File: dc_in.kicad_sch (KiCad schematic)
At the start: 4 parts

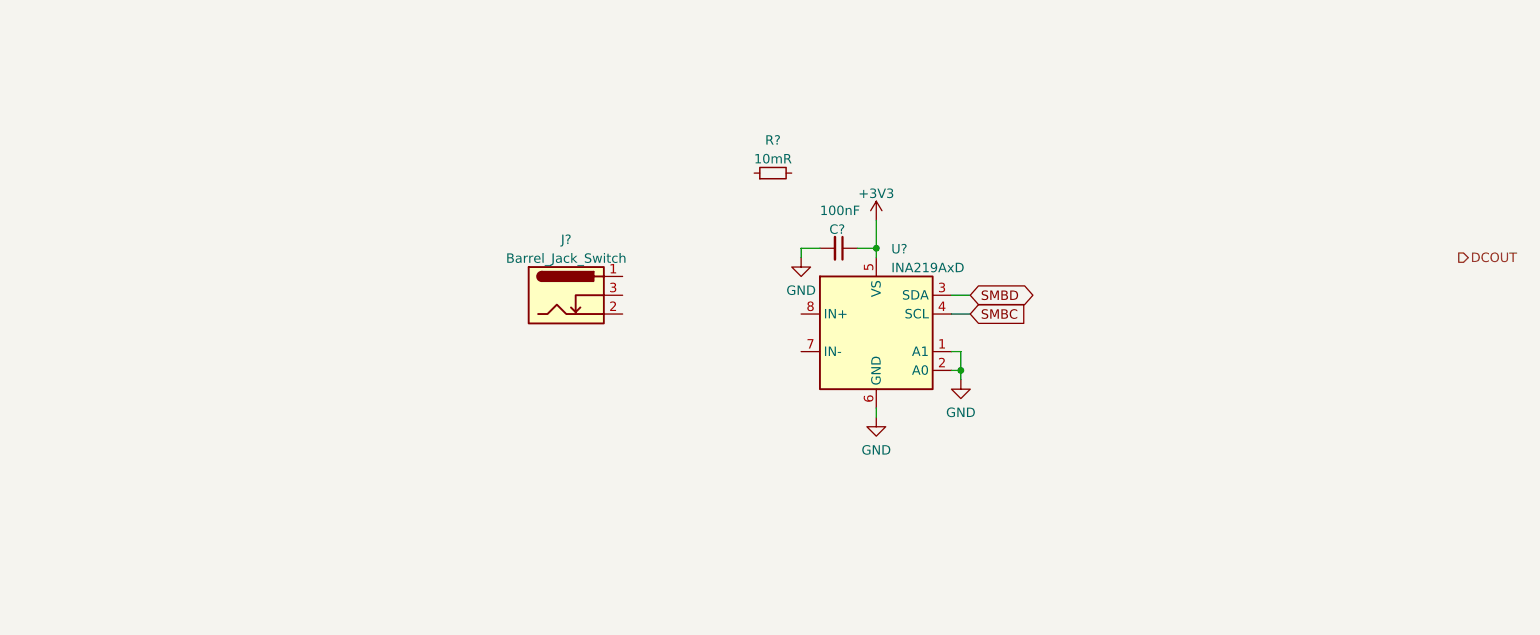
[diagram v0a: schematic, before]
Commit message: Add partial DC output circuitry
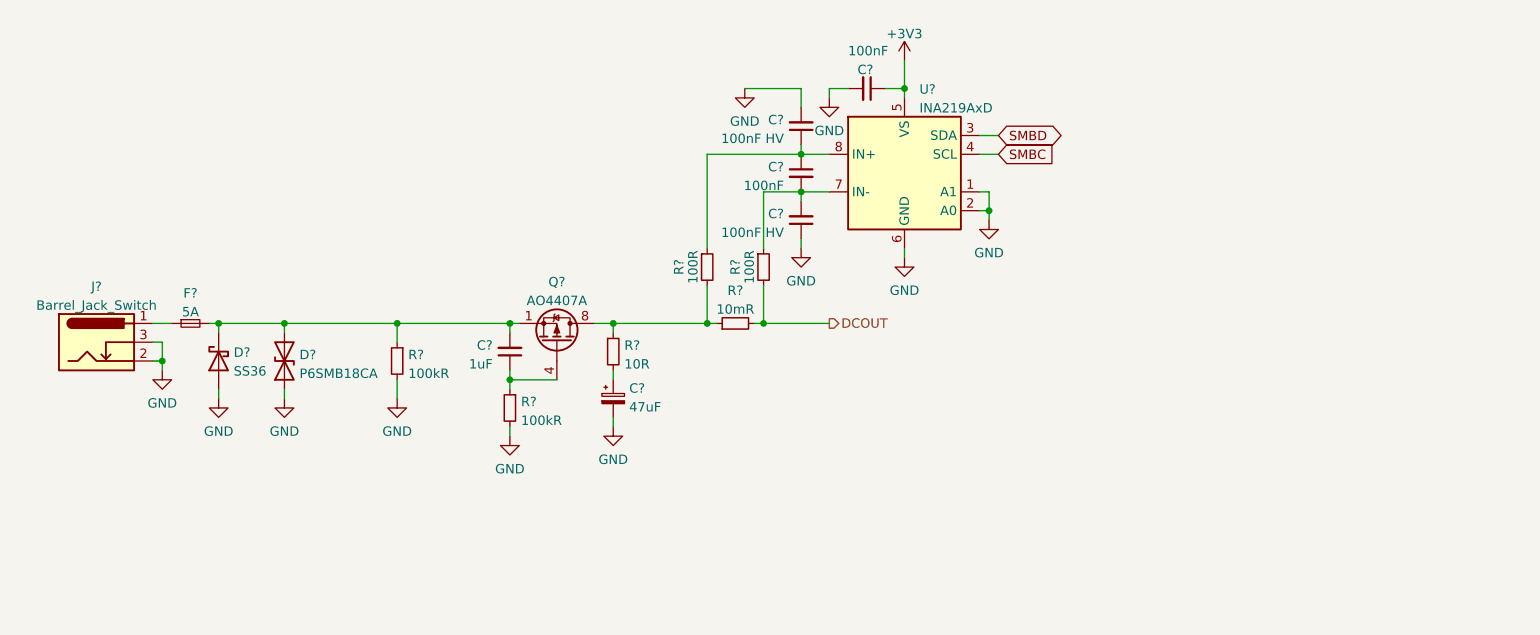
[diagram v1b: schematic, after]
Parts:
- added C? (x2): 100nF HV, Capacitor_SMD:C_0603_1608Metric, symbol Device:C_Small
- added C?: 100nF, Capacitor_SMD:C_0402_1005Metric, symbol Device:C_Small
- added C?: 1uF, Capacitor_SMD:C_0402_1005Metric, symbol Device:C_Small
- added C?: 47uF, Capacitor_SMD:CP_Elec_6.3x5.4, symbol Device:C_Polarized_Small
- added D?: P6SMB18CA, Diode_SMD:D_SMB, symbol Device:D_TVS
- added D?: SS36, Diode_SMD:D_SMC, symbol Device:D_Schottky
- added F?: 5A, Fuse:Fuse_1206_3216Metric, symbol Device:Fuse_Small
- added Q?: AO4407A, Package_SO:SOIC-8_3.9x4.9mm_P1.27mm, symbol Transistor_FET:FDS9435A
- added R? (x2): 100kR, Resistor_SMD:R_0402_1005Metric, symbol Device:R_Small
- added R? (x2): 100R, Resistor_SMD:R_0402_1005Metric, symbol Device:R_Small
- added R?: 10R, Resistor_SMD:R_1206_3216Metric, symbol Device:R_Small
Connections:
- net DCOUT: now also R?.2, R?.2
- net GND: now also J?.2, J?.3, C?.1, C?.2, C?.2, D?.1 (A1), D?.2 (A), R?.2, R?.2
- net at J?.1: now also F?.1
- net at U?.7 (IN-): now also C?.2, C?.2, R?.1
- net at U?.8 (IN+): now also C?.1, C?.1, R?.1
- net at R?.1: now also Q?.5 (D), Q?.6 (D), Q?.7 (D), Q?.8 (D), R?.1, R?.2
- new net: C?.1, Q?.4 (G), R?.1
- new net: C?.2, D?.1 (K), D?.2 (A2), F?.2, Q?.1 (S), Q?.2 (S), Q?.3 (S), R?.1
- new net: C?.1, R?.2
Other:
- moved on the sheet: C?, J?, R?, U?

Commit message: Finish DC output schematic capture
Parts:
- removed C?: 47uF, Capacitor_SMD:CP_Elec_6.3x5.4, symbol Device:C_Polarized_Small
- removed U?: INA219AxD, Package_SO:SOIC-8_3.9x4.9mm_P1.27mm, symbol Analog_ADC:INA219AxD
- added C?: 220uF, Capacitor_SMD:CP_Elec_6.3x7.7, symbol Device:C_Polarized_Small
- added U?: INA219AxD, Package_SO:SOIC-8_3.9x4.9mm_P1.27mm, symbol Analog_ADC:INA219AxD
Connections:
- net +3V3: now also U?.5 (VS)
- net GND: now also C?.2, U?.1 (A1), U?.2 (A0), U?.6 (GND)
- net SMBC: now also U?.4 (SCL)
- net SMBD: now also U?.3 (SDA)
- net at C?.2, C?.2, R?.1: now also U?.7 (IN-)
- net at C?.1, C?.1, R?.1: now also U?.8 (IN+)
- net at R?.2: now also C?.1
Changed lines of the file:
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@@
     (pin "2")
-  )
-  (symbol (lib_id "Connector:Barrel_Jack_Switch") (at 34.29 97.79 0) (unit 1)
-    (in_bom yes) (on_board yes) (fields_autoplaced)
-    (property "Reference" "J?" (id 0) (at 34.29 90.2802 0))
-    (property "Value" "Barrel_Jack_Switch" (id 1) (at 34.29 92.8171 0))
-    (property "Footprint" "" (id 2) (at 35.56 98.806 0)
-      (effects (font (size 1.27 1.27)) hide)
-    )
-    (property "Datasheet" "~" (id 3) (at 35.56 98.806 0)
-      (effects (font (size 1.27 1.27)) hide)
-    )
-    (pin "1")
-    (pin "2")
-    (pin "3")
   )
   (symbol (lib_id "Analog_ADC:INA219AxD") (at 143.51 74.93 0) (unit 1)
@@
     )
     (property "Datasheet" "http://www.ti.com/lit/ds/symlink/ina219.pdf" (id 3) (at 152.4 77.47 0)
+      (effects (font (size 1.27 1.27)) hide)
+    )
+    (property "LCSC" "C138706" (id 4) (at 143.51 74.93 0)
       (effects (font (size 1.27 1.27)) hide)
     )
@@
     (pin "8")
   )
+  (symbol (lib_id "Connector:Barrel_Jack_Switch") (at 34.29 97.79 0) (unit 1)
+    (in_bom yes) (on_board yes) (fields_autoplaced)
+    (property "Reference" "J?" (id 0) (at 34.29 90.2802 0))
+    (property "Value" "Barrel_Jack_Switch" (id 1) (at 34.29 92.8171 0))
+    (property "Footprint" "" (id 2) (at 35.56 98.806 0)
+      (effects (font (size 1.27 1.27)) hide)
+    )
+    (property "Datasheet" "~" (id 3) (at 35.56 98.806 0)
+      (effects (font (size 1.27 1.27)) hide)
+    )
+    (pin "1")
+    (pin "2")
+    (pin "3")
+  )
   (symbol (lib_id "power:GND") (at 104.14 109.22 0) (unit 1)
     (in_bom yes) (on_board yes) (fields_autoplaced)
@@
     (pin "1")
   )
+  (symbol (lib_id "Device:C_Polarized_Small") (at 104.14 105.41 0) (unit 1)
+    (in_bom yes) (on_board yes) (fields_autoplaced)
+    (property "Reference" "C?" (id 0) (at 106.299 104.0292 0)
+      (effects (font (size 1.27 1.27)) (justify left))
+    )
+    (property "Value" "220uF" (id 1) (at 106.299 106.5661 0)
+      (effects (font (size 1.27 1.27)) (justify left))
+    )
+    (property "Footprint" "Capacitor_SMD:CP_Elec_6.3x7.7" (id 2) (at 104.14 105.41 0)
+      (effects (font (size 1.27 1.27)) hide)
+    )
+    (property "Datasheet" "https://datasheet.lcsc.com/lcsc/1912111437_Nichicon-UCM1E221MCL1GS_C340768.pdf" (id 3) (at 104.14 105.41 0)
+      (effects (font (size 1.27 1.27)) hide)
+    )
+    (property "LCSC" "C340768" (id 4) (at 104.14 105.41 0)
+      (effects (font (size 1.27 1.27)) hide)
+    )
+    (pin "1")
+    (pin "2")
+  )
   (symbol (lib_id "power:GND") (at 143.51 86.36 0) (unit 1)
     (in_bom yes) (on_board yes) (fields_autoplaced)
@@
     (pin "1")
   )
-  (symbol (lib_id "Device:C_Polarized_Small") (at 104.14 105.41 0) (unit 1)
-    (in_bom yes) (on_board yes) (fields_autoplaced)
-    (property "Reference" "C?" (id 0) (at 106.299 104.0292 0)
-      (effects (font (size 1.27 1.27)) (justify left))
-    )
-    (property "Value" "47uF" (id 1) (at 106.299 106.5661 0)
-      (effects (font (size 1.27 1.27)) (justify left))
-    )
-    (property "Footprint" "Capacitor_SMD:CP_Elec_6.3x5.4" (id 2) (at 104.14 105.41 0)
-      (effects (font (size 1.27 1.27)) hide)
-    )
-    (property "Datasheet" "https://datasheet.lcsc.com/lcsc/2010160904_ROQANG-RVT1V470M0605_C72522.pdf" (id 3) (at 104.14 105.41 0)
-      (effects (font (size 1.27 1.27)) hide)
-    )
-    (property "LCSC" "C72522" (id 4) (at 104.14 105.41 0)
-      (effects (font (size 1.27 1.27)) hide)
-    )
-    (pin "1")
-    (pin "2")
-  )
   (symbol (lib_id "power:GND") (at 59.69 105.41 0) (unit 1)

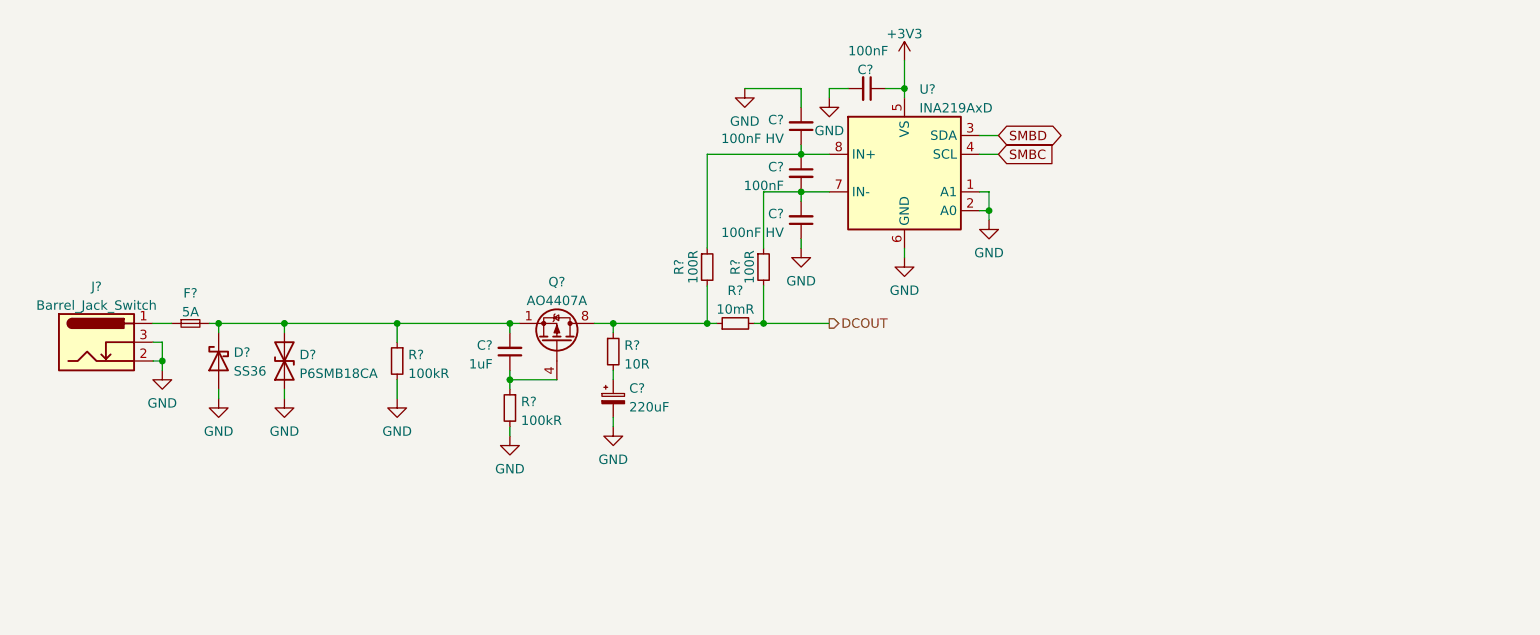
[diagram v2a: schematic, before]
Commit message: Add barrel jack footprints
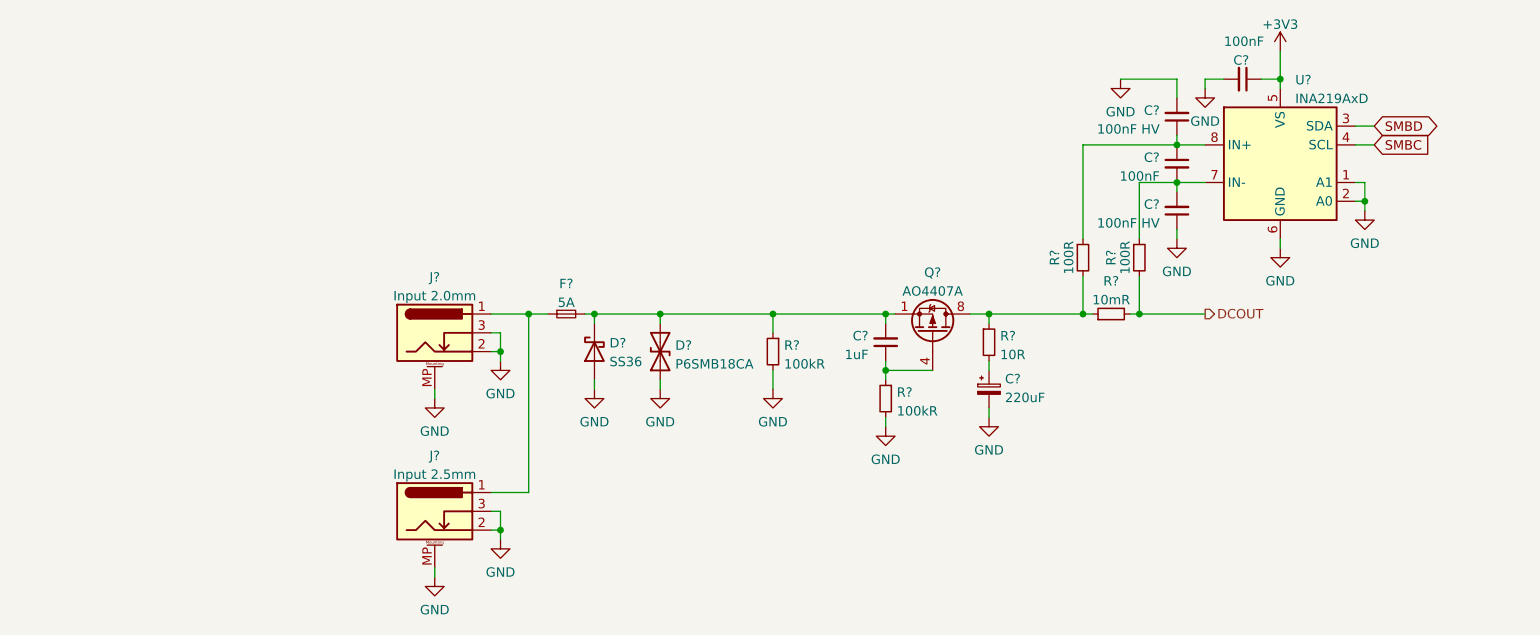
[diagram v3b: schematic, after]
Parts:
- removed J?: Barrel_Jack_Switch, symbol Connector:Barrel_Jack_Switch
- added J?: Input 2.0mm, Connector_BarrelJack_LCSC:BarrelJack_2.0mm_DC-044B, symbol Connector:Barrel_Jack_Switch_MountingPin
- added J?: Input 2.5mm, Connector_BarrelJack_LCSC:BarrelJack_2.0mm_DC-044B, symbol Connector:Barrel_Jack_Switch_MountingPin
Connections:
- net GND: now also J?.2, J?.2, J?.3, J?.3, J?.MP (MountPin), J?.MP (MountPin)
- net at F?.1: now also J?.1, J?.1
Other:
- moved on the sheet: C?, D?, F?, Q?, R?, U?

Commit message: Add individually switchable outputs
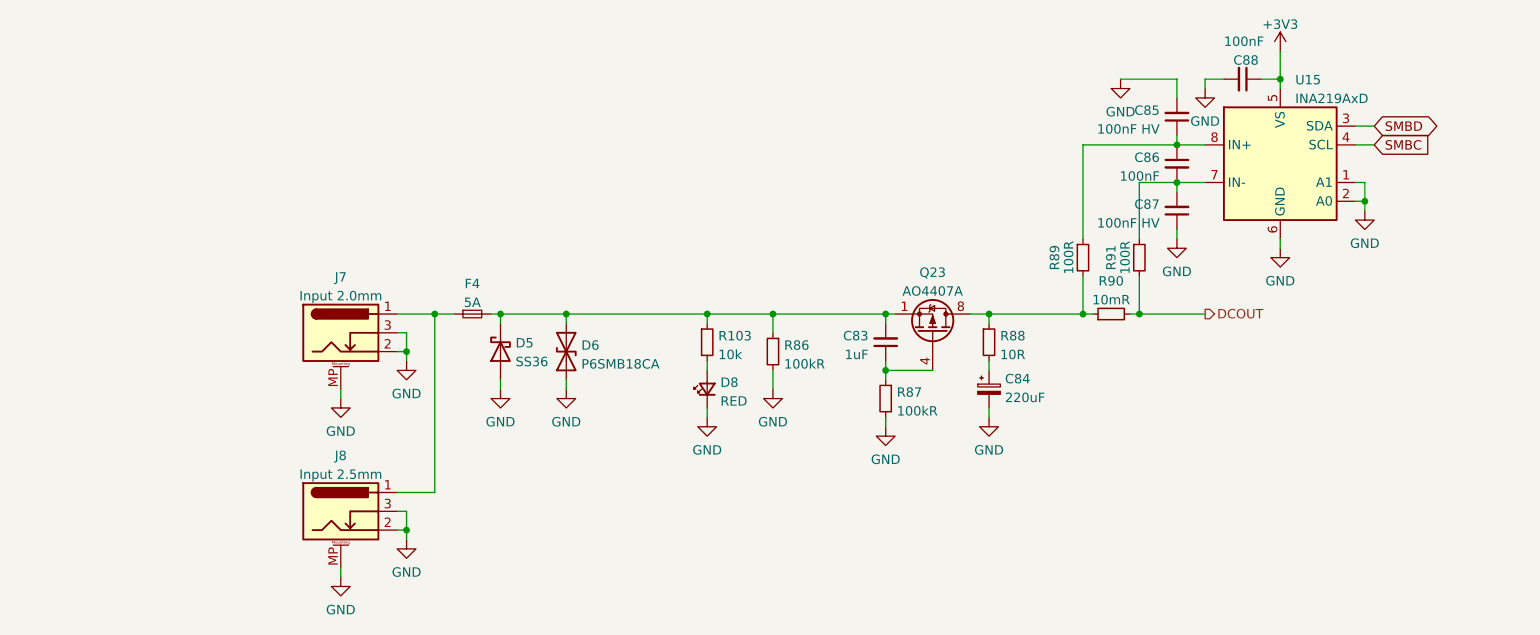
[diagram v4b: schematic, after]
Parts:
- added D8: RED, LED_Indicator:LED_Indicator_RED_MHK1373CRBDT, symbol Device:LED_Small
- added R103: 10k, Resistor_SMD:R_0402_1005Metric, symbol Device:R_Small
- J8: renamed from J?; footprint Connector_BarrelJack_LCSC:BarrelJack_2.0mm_DC-044B -> Connector_BarrelJack_LCSC:BarrelJack_2.5mm_DC-044K-D025
- gave numbers to parts that had none: 18
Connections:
- net GND: now also D8.1 (K)
- net at C83.2, D5.1 (K), D6.2 (A2)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: now also R103.1
- new net: D8.2 (A), R103.2
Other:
- moved on the sheet: D5, D6, F4, J7, J8

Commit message: Partial layout
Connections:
- net DCSMOOTH: now reaches Q23.5 (D), Q23.6 (D), Q23.7 (D), Q23.8 (D), R88.1, R89.2, R90.1
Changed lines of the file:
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@@
     (stroke (width 0) (type default) (color 0 0 0 0))
+  )
+  (label "DCSMOOTH" (at 154.94 93.98 0)
+    (effects (font (size 1.27 1.27)) (justify left bottom))
   )
   (global_label "SMBD" (shape bidirectional) (at 207.01 68.58 0) (fields_autoplaced)

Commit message: Fix footprint origins for JLC assembly
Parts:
- Q23: LCSC C16072 -> C35349
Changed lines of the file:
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@@
       (effects (font (size 1.27 1.27) italic) (justify left) hide)
     )
-    (property "Datasheet" "https://datasheet.lcsc.com/szlcsc/Alpha-Omega-Semicon-AOS-AO4407A_C16072.pdf" (id 3) (at 147.32 96.52 90)
+    (property "Datasheet" "https://datasheet.lcsc.com/szlcsc/Alpha-Omega-Semicon-AOS-AO4407A_C35349.pdf" (id 3) (at 147.32 96.52 90)
       (effects (font (size 1.27 1.27)) (justify left) hide)
     )
-    (property "LCSC" "C16072" (id 4) (at 147.32 96.52 0)
+    (property "LCSC" "C35349" (id 4) (at 147.32 96.52 0)
       (effects (font (size 1.27 1.27)) hide)
     )

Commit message: Fix incorrect AO447A partnumber
The previous partnumber was pointing to a N-Channel MOSFET.
Use a P-Channel one.
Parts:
- Q23: LCSC C35349 -> C167517
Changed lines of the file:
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@@
       (effects (font (size 1.27 1.27)) (justify left) hide)
     )
-    (property "LCSC" "C35349" (id 4) (at 147.32 96.52 0)
+    (property "LCSC" "C167517" (id 4) (at 147.32 96.52 0)
       (effects (font (size 1.27 1.27)) hide)
     )

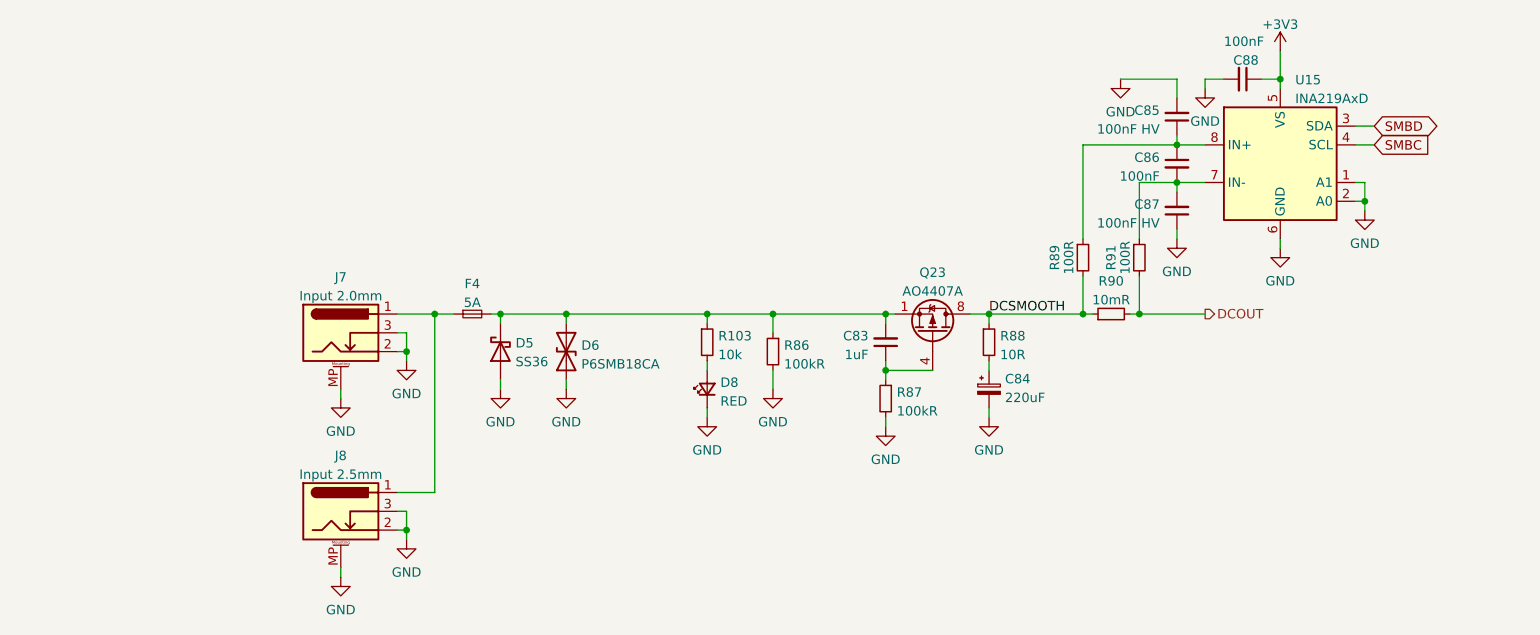
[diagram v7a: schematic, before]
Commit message: Rev 1.0 bugfixes
Changes:
 - Replace DCOK-driven DC passthrough switch with ideal diode
 - Reduce INA219 series filter resistance to 1 ohm
 - Simplify debug USB power gating
 - Fix incorrect USB CC pullups
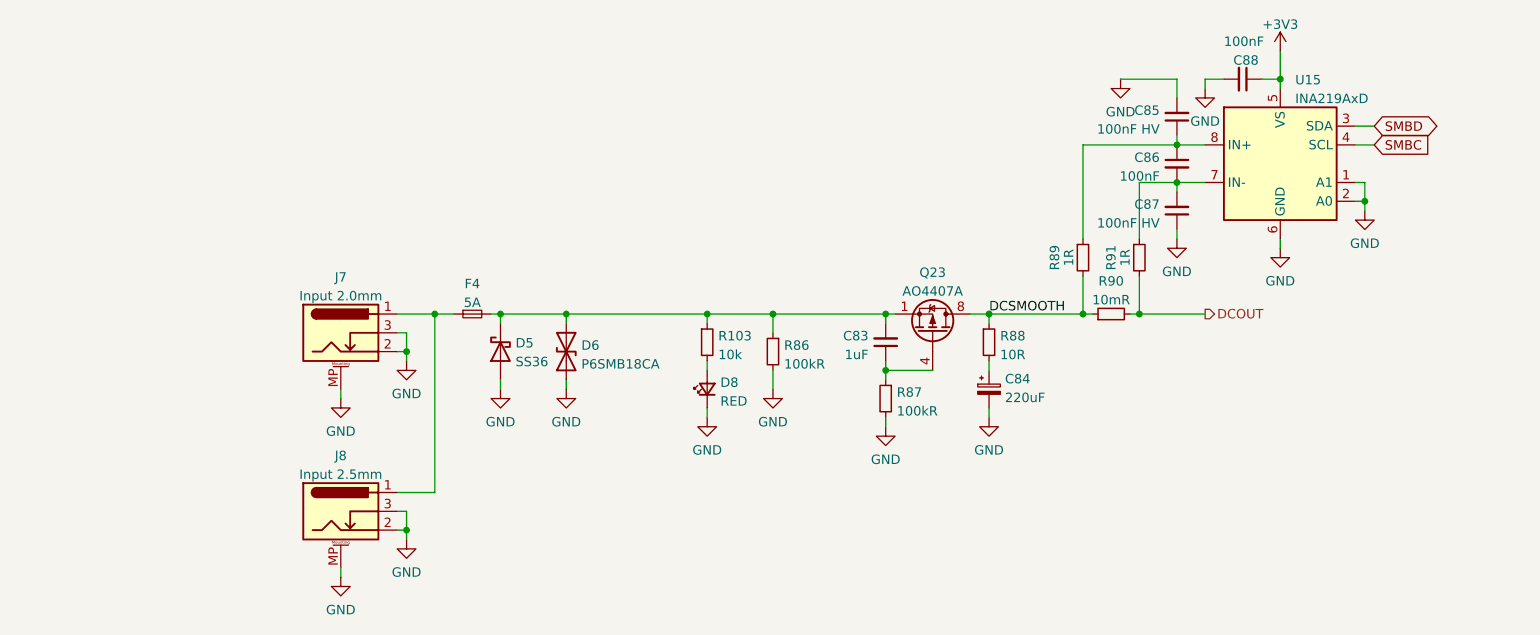
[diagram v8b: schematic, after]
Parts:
- R89, R91: value 100R -> 1R; LCSC C25076 -> C25086
